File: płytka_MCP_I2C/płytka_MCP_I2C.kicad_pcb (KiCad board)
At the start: 2 copper layers, 98 x 77 mm, 33 parts, among them J1 A0, J10 V0, J11 Ext, J12 I2C, J13 U2, J15 U2, J16 U3, J17 RS, J18 K, J19 A, J2 A1, J20 VDD, J21 GND, J23 VSS, J24 Conn_01x16_Pin, J25 LCD, J26 VCC, J3 A2, J4 SDA, J5 SCL, J6 INTA, J7 INTB, J8 INTA, J9 RESET, U1 MCP23017_SP

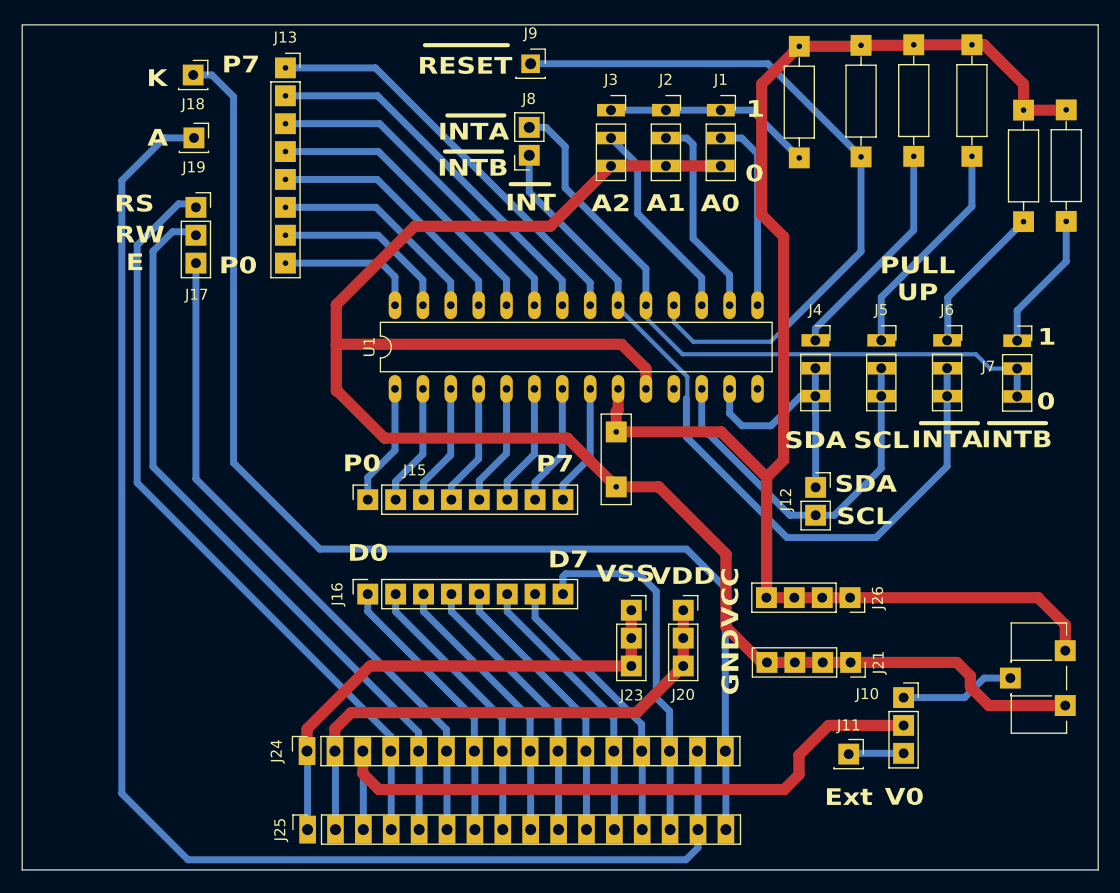
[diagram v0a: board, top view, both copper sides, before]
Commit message: _MCP_I2C płytka do zmniejszenia
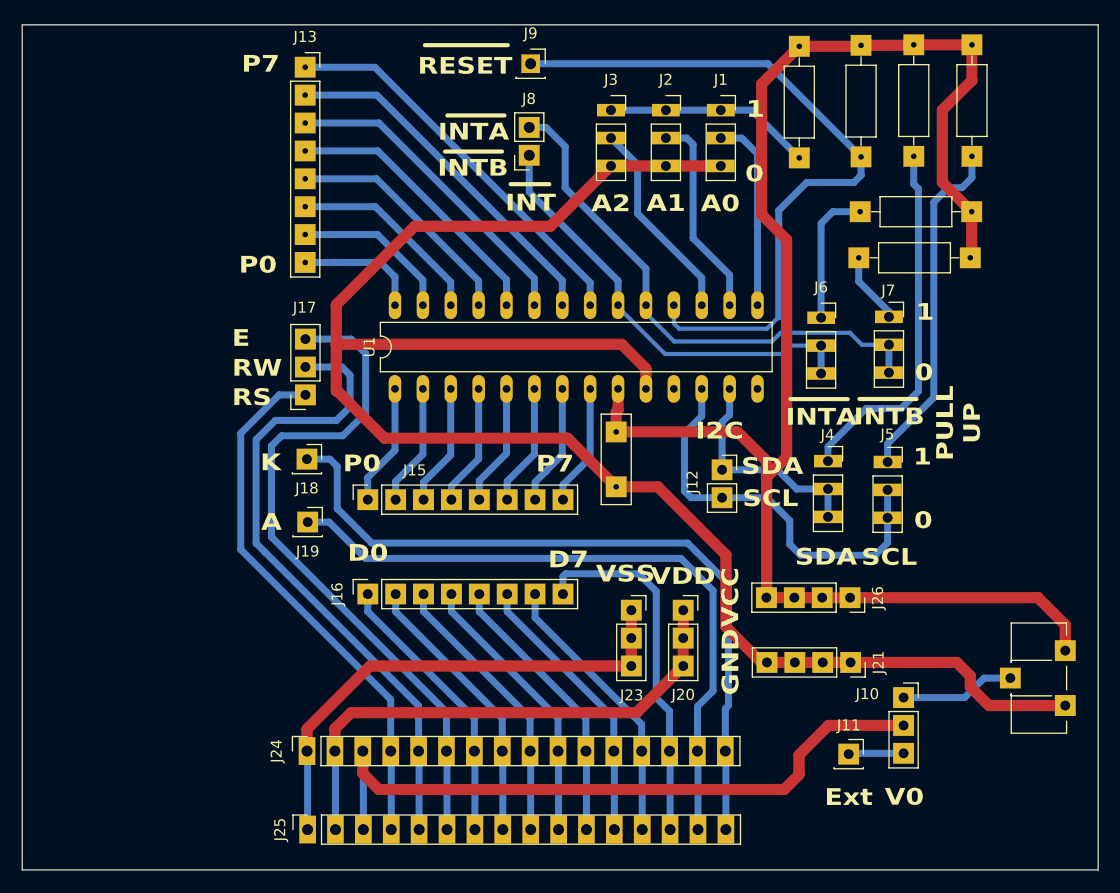
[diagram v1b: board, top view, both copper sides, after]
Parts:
- moved J19 36.5 mm to (61.6, 83.6)
- moved J18 36.5 mm to (61.5, 77.9)
- moved J17 19.8 mm to (61.4, 72.1), turned to 180 degrees
- moved R5 16.1 mm to (122.0, 59.6), turned to 180 degrees
- moved J7 11.9 mm to (114.5, 65.0)
- moved J6 11.7 mm to (108.4, 65.0)
- moved J5 11.1 mm to (114.4, 78.2)
- moved J4 11.1 mm to (109.0, 78.1)
- moved R4 10.4 mm to (122.1, 55.4), turned to 180 degrees
- moved J12 8.67 mm to (99.3, 78.9)
- moved J13 1.80 mm to (61.4, 42.2)
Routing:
- net Net-(J19-Pin_1): track 128.3 -> 61.9 mm
- net Net-(J18-Pin_1): track 109.4 -> 67.8 mm
- net Net-(J6-Pin_2): track 70.9 -> 40.2 mm
- net Net-(J17-Pin_1): track 69.7 -> 49.1 mm
- net Net-(J4-Pin_1): track 20.5 -> 33.2 mm
- net Net-(J5-Pin_1): track 20.2 -> 31.8 mm
- net Net-(J7-Pin_2): track 60.9 -> 49.6 mm
- net VCC: track 131.3 -> 141.7 mm
- net Net-(J17-Pin_2): track 67.4 -> 58.7 mm
- net Net-(J7-Pin_1): track 12.8 -> 6.52 mm
- net Net-(J12-Pin_2): track 34.0 -> 37.4 mm
- net Net-(J12-Pin_1): track 22.5 -> 20.6 mm
- net Net-(J13-Pin_3): track 31.0 -> 29.2 mm
- net Net-(J13-Pin_6): track 20.0 -> 18.2 mm
- net Net-(J13-Pin_5): track 23.6 -> 21.9 mm
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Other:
- board text added: "I2C"

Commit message: Korekcja rozmiaru płytki, utworzenie draftow, do druku
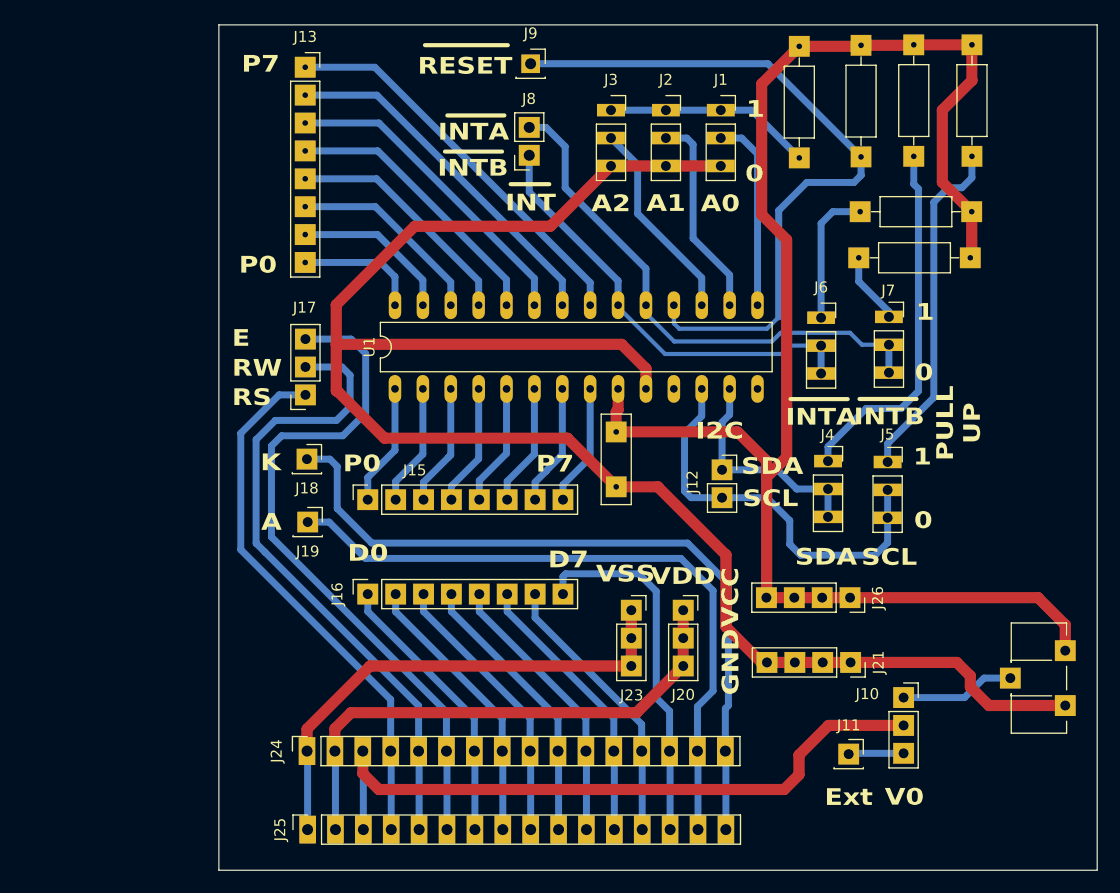
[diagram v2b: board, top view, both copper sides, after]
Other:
- board size 98 x 77 mm -> 80 x 77 mm
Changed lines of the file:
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@@
 		(layer "F.SilkS")
-	)
-	(gr_circle
-		(center 129.65 111.9)
-		(end 130.9 112.9)
-		(stroke
-			(width 0.1)
-			(type default)
-		)
-		(fill no)
-		(layer "Dwgs.User")
 	)
 	(gr_rect
@@
 	)
 	(gr_circle
-		(center 40.15 111.55)
-		(end 40.925 112.95)
+		(center 125.64 45)
+		(end 127.240781 45)
 		(stroke
 			(width 0.1)
-			(type default)
-		)
-		(fill no)
+			(type solid)
+		)
+		(fill no)
+		(locked yes)
 		(layer "Dwgs.User")
 	)
@@
 	)
 	(gr_circle
-		(center 129.36 41.97)
-		(end 129.76 43.52)
+		(center 125.64 111.61)
+		(end 127.240781 111.61)
+		(stroke
+			(width 0.1)
+			(type solid)
+		)
+		(fill no)
+		(locked yes)
+		(layer "Dwgs.User")
+	)
+	(gr_circle
+		(center 56.489805 45)
+		(end 58.09 45)
+		(stroke
+			(width 0.1)
+			(type solid)
+		)
+		(fill no)
+		(locked yes)
+		(layer "Dwgs.User")
+	)
+	(gr_circle
+		(center 56.489805 111.61)
+		(end 57.264805 113.01)
 		(stroke
 			(width 0.1)
@@
 		(layer "Dwgs.User")
 	)
-	(gr_circle
-		(center 56.49 111.625)
-		(end 57.265 113.025)
-		(stroke
-			(width 0.1)
-			(type default)
-		)
-		(fill no)
-		(layer "Dwgs.User")
-	)
-	(gr_circle
-		(center 40.635 41.995195)
-		(end 41.41 43.395195)
-		(stroke
-			(width 0.1)
-			(type default)
-		)
-		(fill no)
-		(locked yes)
-		(layer "Dwgs.User")
-	)
 	(gr_rect
-		(start 35.6 38.355)
-		(end 133.6 115.325)
+		(start 53.51 38.355)
+		(end 133.51 115.355)
 		(stroke
 			(width 0.05)
@@
 		(layer "Dwgs.User")
 		(pts
-			(xy 35.6 38.355) (xy 133.6 38.355)
-		)
-		(height -16.985)
+			(xy 53.51 38.355) (xy 133.51 38.355)
+		)
+		(height -4.355)
 		(orientation 0)
 		(format
@@
 			(keep_text_aligned yes)
 		)
-		(gr_text "98"
-			(at 84.6 20.22 0)
-			(layer "Dwgs.User")
-			(effects
-				(font
-					(size 1 1)
-					(thickness 0.15)
-				)
-			)
-		)
-	)
-	(dimension
-		(type orthogonal)
-		(layer "Dwgs.User")
-		(pts
-			(xy 133.6 38.355) (xy 133.6 115.325)
-		)
-		(height 20.25)
-		(orientation 1)
-		(format
-			(prefix "")
-			(suffix "")
-			(units 3)
-			(units_format 0)
-			(precision 4)
-			(suppress_zeroes yes)
-		)
-		(style
-			(thickness 0.1)
-			(arrow_length 1.27)
-			(text_position_mode 0)
-			(arrow_direction outward)
-			(extension_height 0.58642)
-			(extension_offset 0.5)
-			(keep_text_aligned yes)
-		)
-		(gr_text "76,97"
-			(at 152.7 76.84 90)
+		(gr_text "80"
+			(at 93.51 32.85 0)
 			(layer "Dwgs.User")
 			(effects
@@
 			(layer "Dwgs.User")
 			(effects
+				(font
+					(size 1 1)
+					(thickness 0.15)
+				)
+			)
+		)
+	)
+	(dimension
+		(type orthogonal)
+		(layer "Dwgs.User")
+		(pts
+			(xy 133.51 115.355) (xy 133.51 38.355)
+		)
+		(height 3.59)
+		(orientation 1)
+		(format
+			(prefix "")
+			(suffix "")
+			(units 3)
+			(units_format 0)
+			(precision 4)
+			(suppress_zeroes yes)
+		)
+		(style
+			(thickness 0.1)
+			(arrow_length 1.27)
+			(text_position_mode 0)
+			(arrow_direction outward)
+			(extension_height 0.58642)
+			(extension_offset 0.5)
+			(keep_text_aligned yes)
+		)
+		(gr_text "77"
+			(at 135.95 76.855 90)
+			(layer "Dwgs.User")
+			(effects

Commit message: Wyrownane otwory
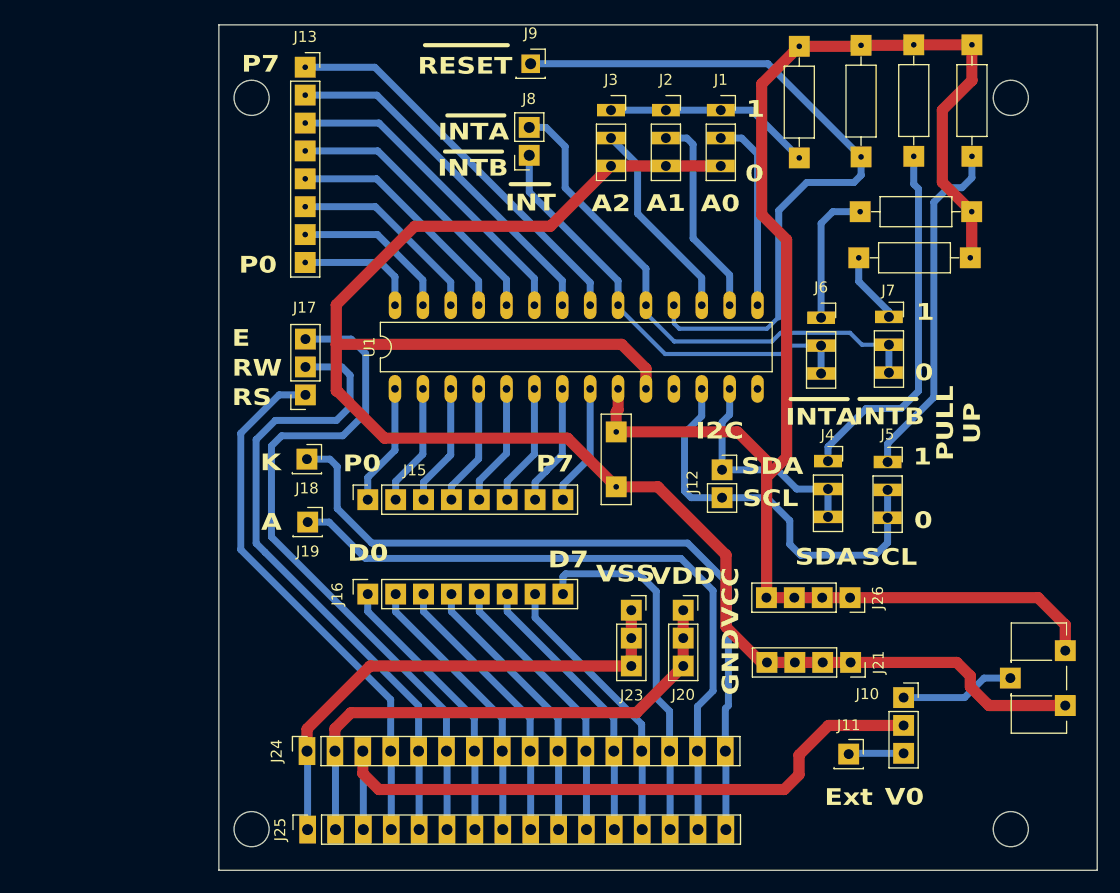
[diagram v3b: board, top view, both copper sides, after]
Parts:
- added ?: , , F.Cu at (56.5, 111.6)
- added ?: , , F.Cu at (56.5, 45.0)
- added ?: , , F.Cu at (125.6, 45.0)
- added ?: , , F.Cu at (125.6, 111.6)
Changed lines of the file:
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@@
 		)
 	)
+	(footprint ""
+		(layer "F.Cu")
+		(at 56.489805 111.61)
+		(property "Reference" ""
+			(at 0 0 0)
+			(layer "F.SilkS")
+			(effects
+				(font
+					(size 1.27 1.27)
+					(thickness 0.15)
+				)
+			)
+		)
+		(property "Value" ""
+			(at 0 0 0)
+			(layer "F.Fab")
+			(effects
+				(font
+					(size 1.27 1.27)
+					(thickness 0.15)
+				)
+			)
+		)
+		(property "Datasheet" ""
+			(at 0 0 0)
+			(layer "F.Fab")
+			(hide yes)
+			(effects
+				(font
+					(size 1.27 1.27)
+					(thickness 0.15)
+				)
+			)
+		)
+		(property "Description" ""
+			(at 0 0 0)
+			(layer "F.Fab")
+			(hide yes)
+			(effects
+				(font
+					(size 1.27 1.27)
+					(thickness 0.15)
+				)
+			)
+		)
+		(pad "" np_thru_hole circle
+			(at 0 0)
+			(size 3.2 3.2)
+			(drill 3.2)
+			(layers "*.Cu" "*.Mask")
+		)
+		(embedded_fonts no)
+	)
+	(footprint ""
+		(layer "F.Cu")
+		(at 56.489805 45)
+		(property "Reference" ""
+			(at 0 0 0)
+			(layer "F.SilkS")
+			(effects
+				(font
+					(size 1.27 1.27)
+					(thickness 0.15)
+				)
+			)
+		)
+		(property "Value" ""
+			(at 0 0 0)
+			(layer "F.Fab")
+			(effects
+				(font
+					(size 1.27 1.27)
+					(thickness 0.15)
+				)
+			)
+		)
+		(property "Datasheet" ""
+			(at 0 0 0)
+			(layer "F.Fab")
+			(hide yes)
+			(effects
+				(font
+					(size 1.27 1.27)
+					(thickness 0.15)
+				)
+			)
+		)
+		(property "Description" ""
+			(at 0 0 0)
+			(layer "F.Fab")
+			(hide yes)
+			(effects
+				(font
+					(size 1.27 1.27)
+					(thickness 0.15)
+				)
+			)
+		)
+		(pad "" np_thru_hole circle
+			(at 0 0)
+			(size 3.2 3.2)
+			(drill 3.2)
+			(layers "*.Cu" "*.Mask")
+		)
+		(embedded_fonts no)
+	)
 	(footprint "Library:PinSocket_1x03_P2.54mm_Vertical"
 		(layer "F.Cu")
@@
 		)
 	)
+	(footprint ""
+		(layer "F.Cu")
+		(at 125.64 45)
+		(property "Reference" ""
+			(at 0 0 0)
+			(layer "F.SilkS")
+			(effects
+				(font
+					(size 1.27 1.27)
+					(thickness 0.15)
+				)
+			)
+		)
+		(property "Value" ""
+			(at 0 0 0)
+			(layer "F.Fab")
+			(effects
+				(font
+					(size 1.27 1.27)
+					(thickness 0.15)
+				)
+			)
+		)
+		(property "Datasheet" ""
+			(at 0 0 0)
+			(layer "F.Fab")
+			(hide yes)
+			(effects
+				(font
+					(size 1.27 1.27)
+					(thickness 0.15)
+				)
+			)
+		)
+		(property "Description" ""
+			(at 0 0 0)
+			(layer "F.Fab")
+			(hide yes)
+			(effects
+				(font
+					(size 1.27 1.27)
+					(thickness 0.15)
+				)
+			)
+		)
+		(pad "" np_thru_hole circle
+			(at 0 0)
+			(size 3.2 3.2)
+			(drill 3.2)
+			(layers "*.Cu" "*.Mask")
+		)
+		(embedded_fonts no)
+	)
 	(footprint "Library:R_Axial_DIN0207_L6.3mm_D2.5mm_P10.16mm_Horizontal_square"
 		(layer "F.Cu")
@@
 		)
 	)
+	(footprint ""
+		(layer "F.Cu")
+		(at 125.64 111.61)
+		(property "Reference" ""
+			(at 0 0 0)
+			(layer "F.SilkS")
+			(effects
+				(font
+					(size 1.27 1.27)
+					(thickness 0.15)
+				)
+			)
+		)
+		(property "Value" ""
+			(at 0 0 0)
+			(layer "F.Fab")
+			(effects
+				(font
+					(size 1.27 1.27)
+					(thickness 0.15)
+				)
+			)
+		)
+		(property "Datasheet" ""
+			(at 0 0 0)
+			(layer "F.Fab")
+			(hide yes)
+			(effects
+				(font
+					(size 1.27 1.27)
+					(thickness 0.15)
+				)
+			)
+		)
+		(property "Description" ""
+			(at 0 0 0)
+			(layer "F.Fab")
+			(hide yes)
+			(effects
+				(font
+					(size 1.27 1.27)
+					(thickness 0.15)
+				)
+			)
+		)
+		(pad "" np_thru_hole circle
+			(at 0 0)
+			(size 3.2 3.2)
+			(drill 3.2)
+			(layers "*.Cu" "*.Mask")
+		)
+		(embedded_fonts no)
+	)
 	(footprint "Library:PinSocket_1x01_P2.54mm_Vertical_kwadart"
